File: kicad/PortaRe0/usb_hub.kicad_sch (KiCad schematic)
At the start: 85 parts, among them U10 TPS2042BDR, U12 HC-USB3.0-L168-WP, U4 VL812, U5 W25Q32JVSSIQ, U7 TPS61023DRLR, U8 USB31-TYPE-C-FSABC, Y1 C9006

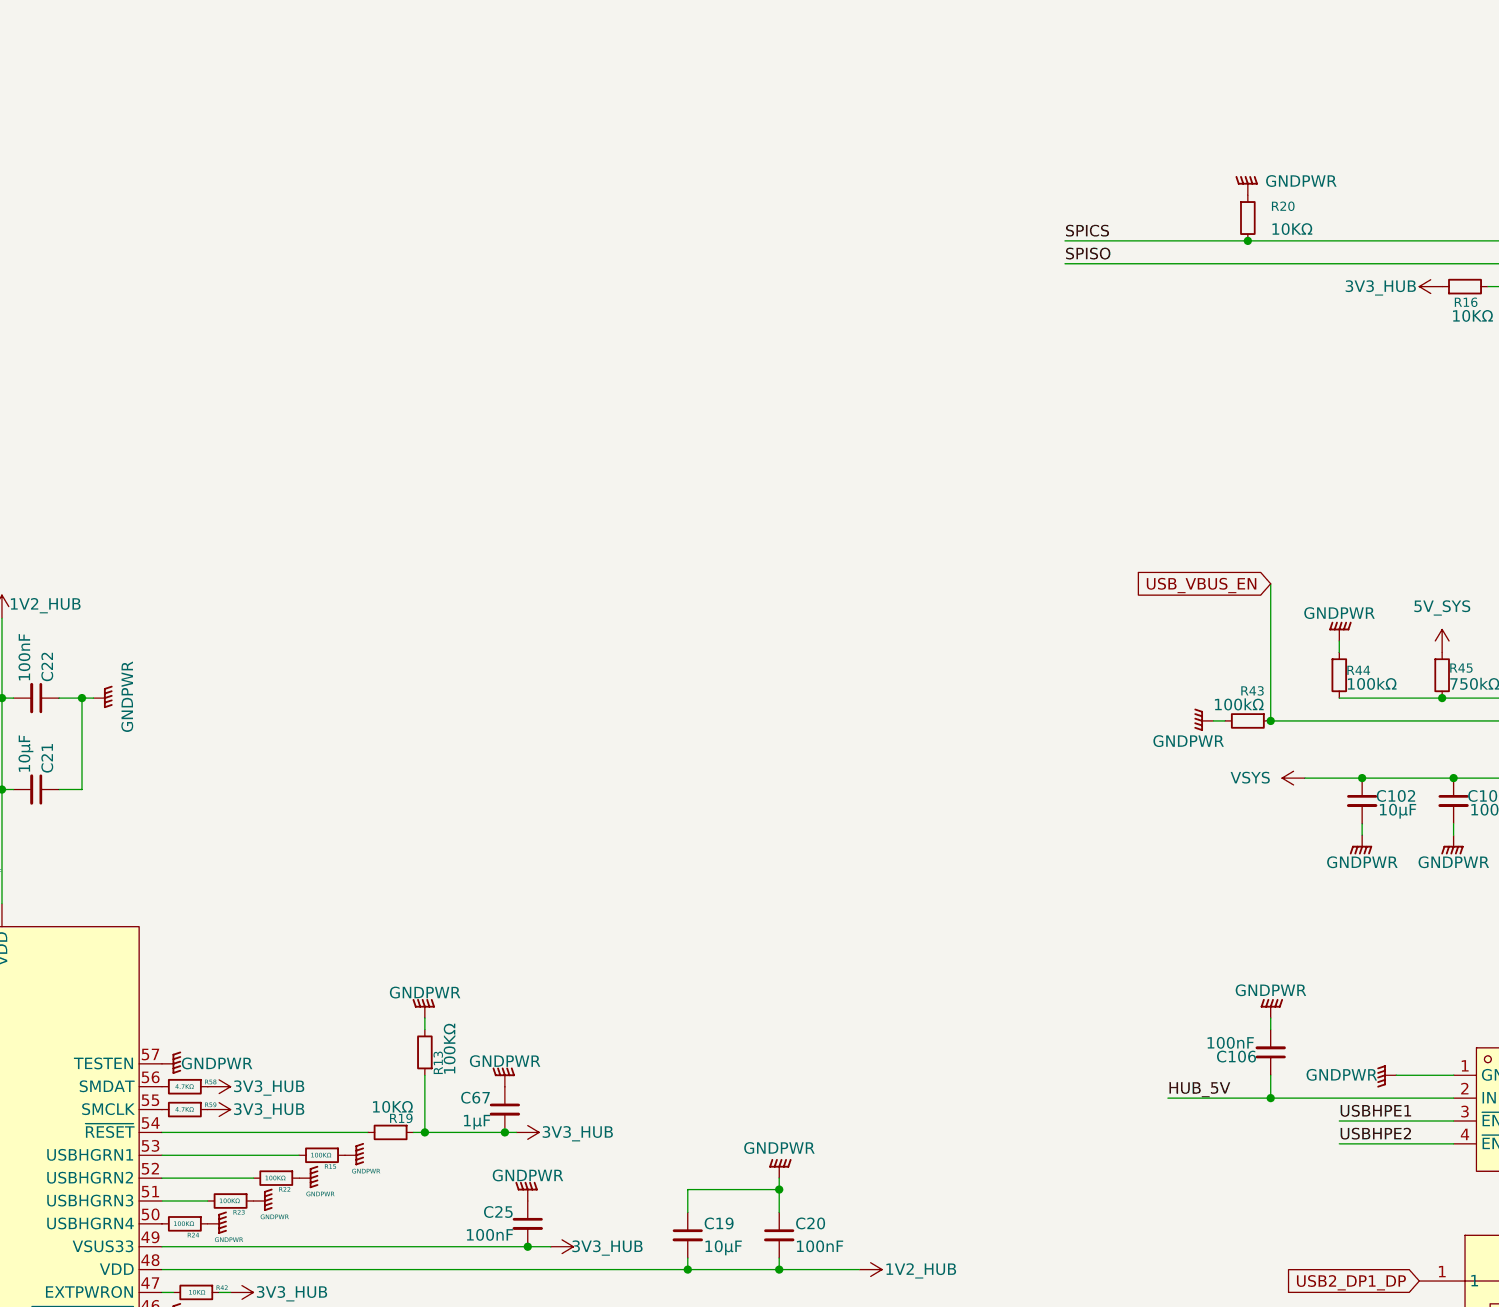
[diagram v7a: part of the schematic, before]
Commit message: KiCad/Docs: チェックシート04-06完了・回路修正(session25)
- VL812: W25Q32 /CS GNDプルダウン→3V3_HUBプルアップ修正
- RP2040 #1/#2: クリスタルシンボル GND23→GND24 修正
- RP2040 #1: GP24/GP25 接続追加
- チェックシート04(VL812)/05(RP2040 kbd)/06(RP2040 audio)記入完了

Co-Authored-By: Claude Sonnet 4.6 <noreply@anthropic.com>
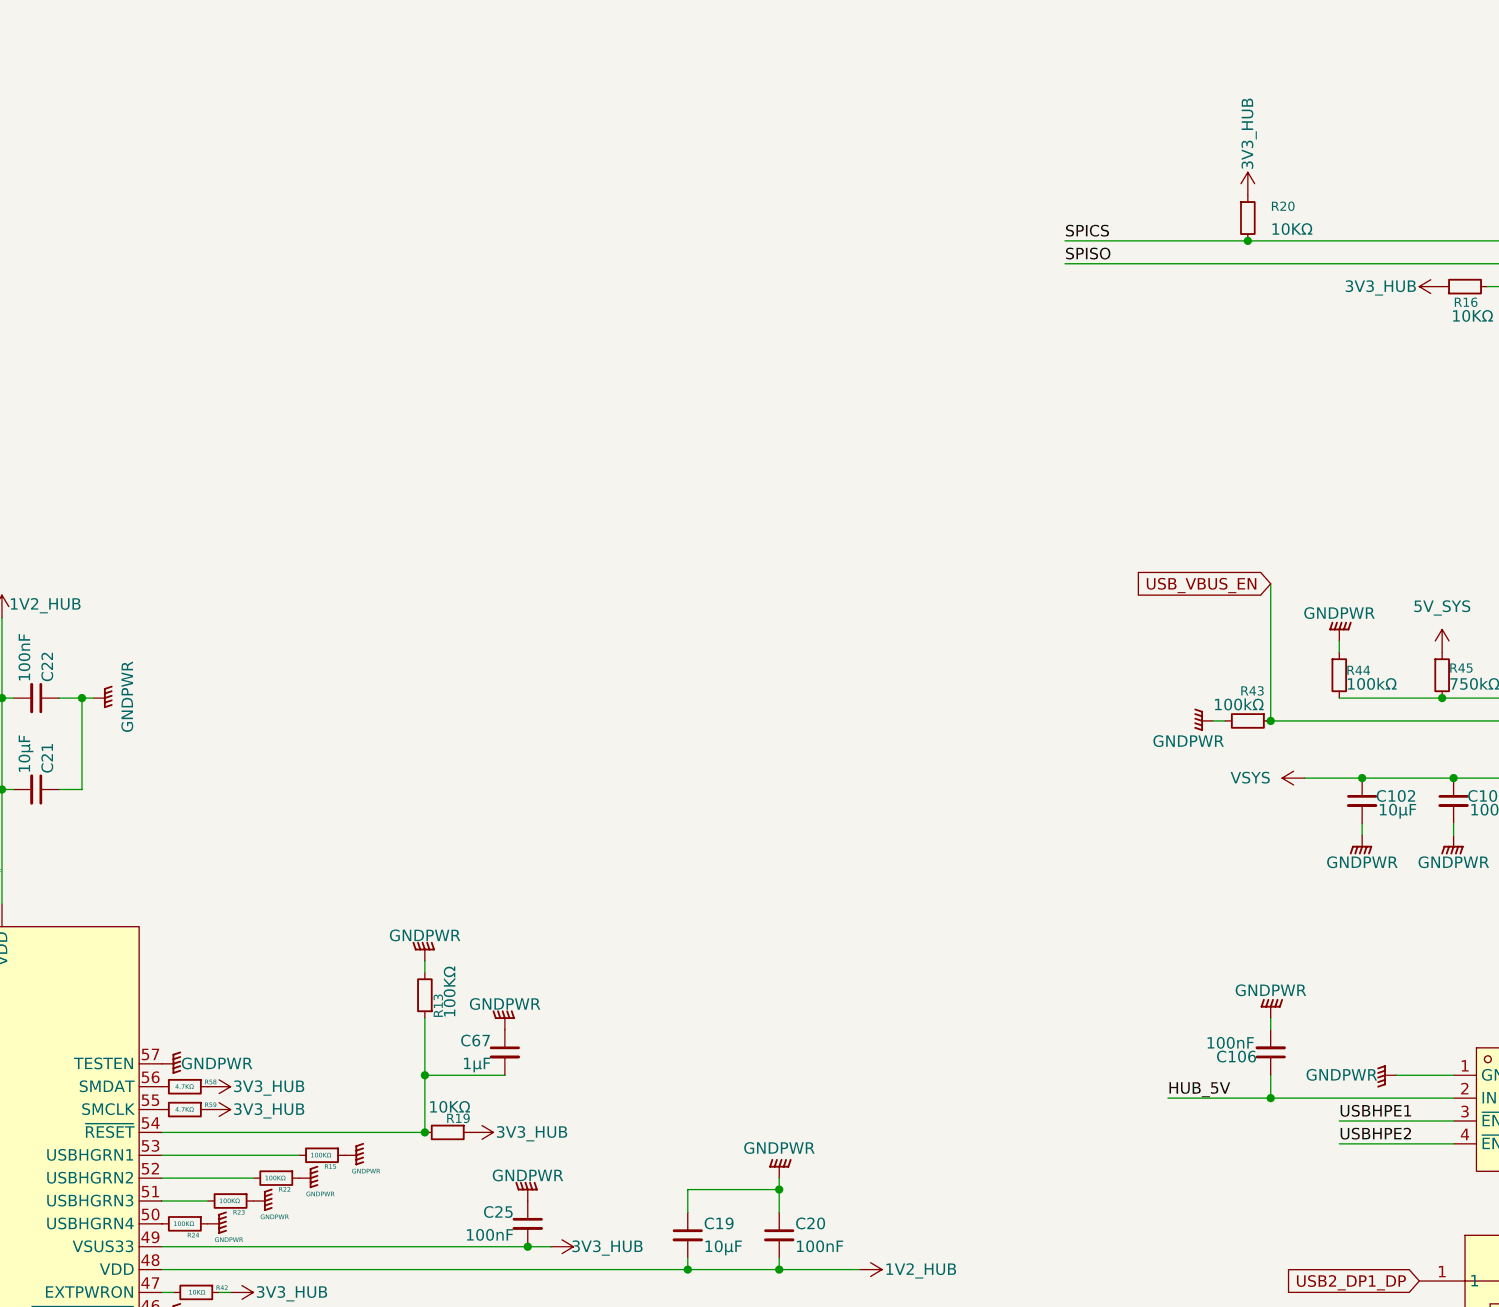
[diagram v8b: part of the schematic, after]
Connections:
- net 3V3_HUB: now also R20.1; no longer C67.2, R13.1
- net GNDPWR: no longer R20.1
- net at R19.2, U4.54 (~{RESET}): now also C67.2, R13.1
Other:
- moved on the sheet: C67, R13, R19
